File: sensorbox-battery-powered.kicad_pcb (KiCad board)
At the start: 2 copper layers, 30 x 55 mm, 21 parts, among them J1 Conn_01x02, J2 Conn_01x06_Male, SW1 Reset, SW2 Program, U1 ESP-12F, U2 BME280

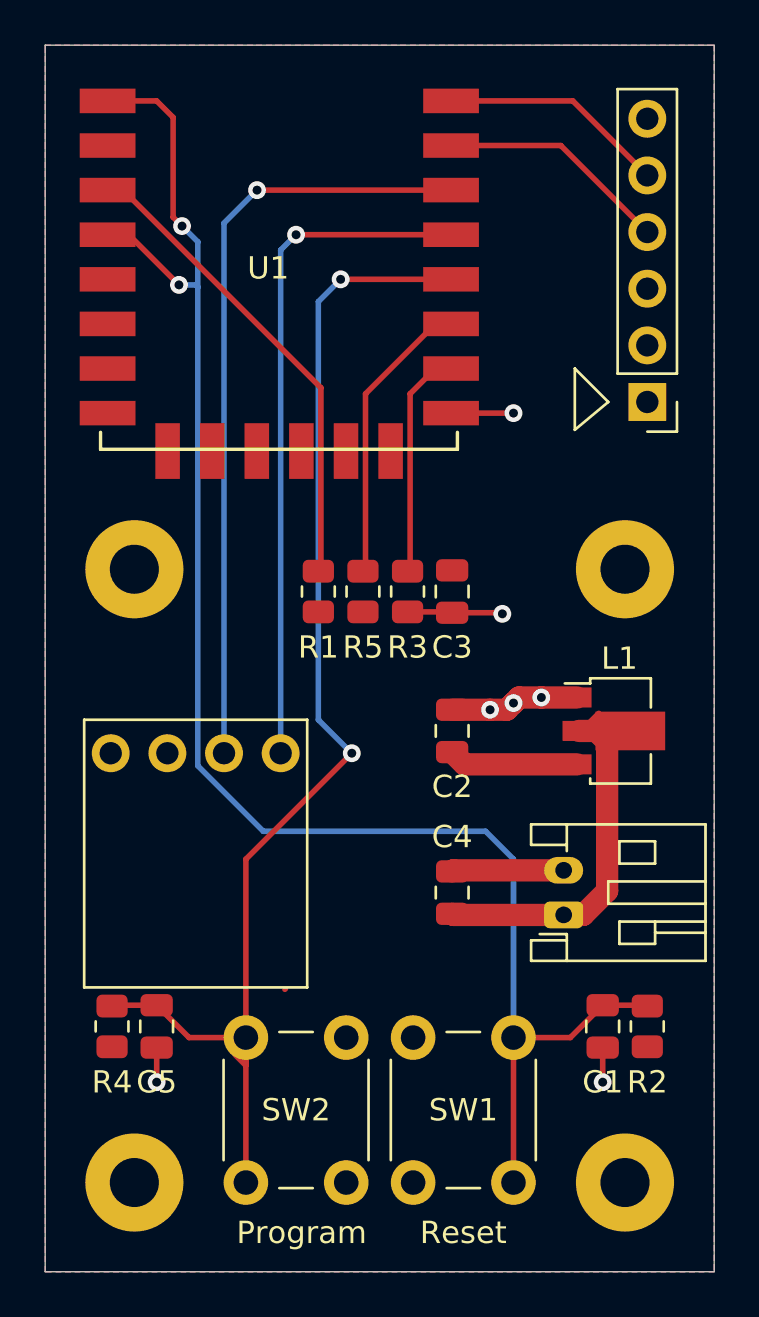
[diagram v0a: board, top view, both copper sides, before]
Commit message: Add battery sensing circuit.
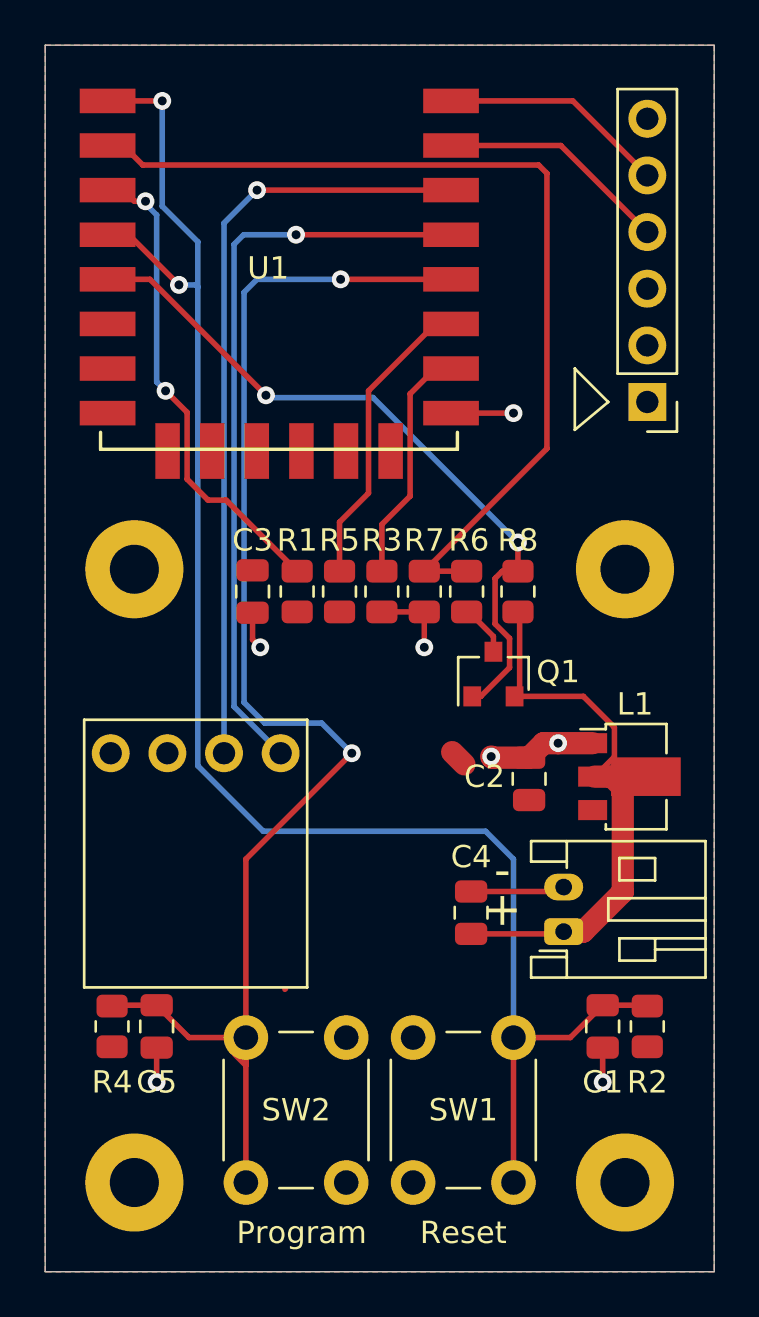
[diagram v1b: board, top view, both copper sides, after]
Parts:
- added Q1: AO3401A, Package_TO_SOT_SMD:SOT-23, F.Cu at (20.1, 28.2)
- added R6: 33k, Resistor_SMD:R_0805_2012Metric, F.Cu at (18.9, 24.5)
- added R7: 10k, Resistor_SMD:R_0805_2012Metric, F.Cu at (17.0, 24.5)
- added R8: 10k, Resistor_SMD:R_0805_2012Metric, F.Cu at (21.2, 24.5)
- moved C3 8.95 mm to (9.30, 24.5)
- moved C2 4.07 mm to (21.7, 32.9)
- moved L1 2.17 mm to (26.2, 32.8)
- moved C4 1.24 mm to (19.1, 38.9)
- moved R3 1.15 mm to (15.1, 24.5)
- moved R5 1.05 mm to (13.2, 24.5)
- moved R1 0.95 mm to (11.3, 24.5)
- moved J1 0.75 mm to (23.2, 39.8)
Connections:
- net Net-(C4-Pad1) renamed +BATT
- U1 pad 2: Net-(U1-Pad2) -> BAT_SENS
- U1 pad 5: Net-(U1-Pad5) -> ENABLE_BAT_SENS
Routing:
- net BAT_SENS: track 0.00 -> 41.6 mm
- net ENABLE_BAT_SENS: track 0.00 -> 31.5 mm, vias 0 -> 2
- net +BATT: track 16.8 -> 25.5 mm
- net Net-(C5-Pad2): track 57.4 -> 63.9 mm
- net +3V3: track 7.26 -> 1.47 mm
- net SDA: track 29.8 -> 32.9 mm
- net Net-(Q1-Pad3): track 0.00 -> 2.24 mm
- net GND: track 21.7 -> 21.0 mm
- net Net-(R5-Pad2): track 12.8 -> 13.4 mm
- net Net-(R1-Pad1): track 20.8 -> 21.2 mm, vias 0 -> 2
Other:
- board text added: "+"
- board text added: "-"

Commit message: Final design.
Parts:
- J1: footprint Connector_JST:JST_PH_S2B-PH-K_1x02_P2.00mm_Horizontal -> jst-conectors:JST_PH_S2B-PH-SM4-TB_1x02-1MP_P2.00mm_Horizontal
- moved C2 4.54 mm to (17.2, 33.5), turned to 180 degrees
- moved L1 2.94 mm to (25.7, 29.9)
- moved J1 2.71 mm to (24.6, 37.4)
- moved C4 2.41 mm to (17.3, 37.3)
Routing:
- net GND: track 21.0 -> 23.8 mm, vias 7 -> 9
- net +3V3: track 1.47 -> 0.70 mm
